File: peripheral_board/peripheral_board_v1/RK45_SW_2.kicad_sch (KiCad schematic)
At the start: 10 parts

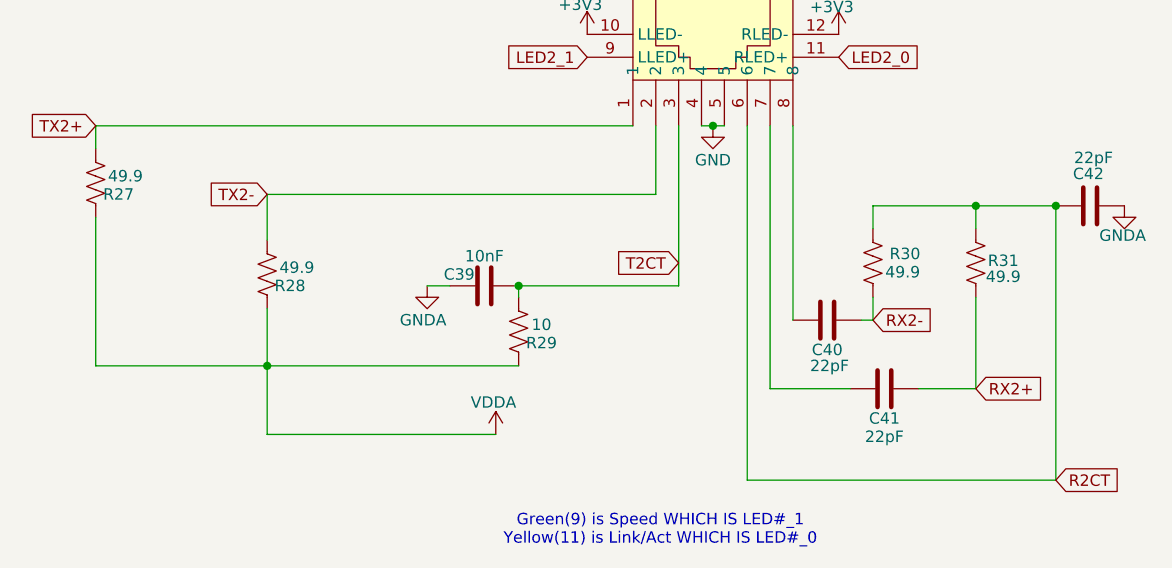
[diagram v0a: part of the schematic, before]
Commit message: Update to the board
Changed the WIZNET configuration to match that of the Pico2 eval board.
Changed the some names and some layout of the page. Not too much besides copying, reading as to why it is they way they made it and then applying.
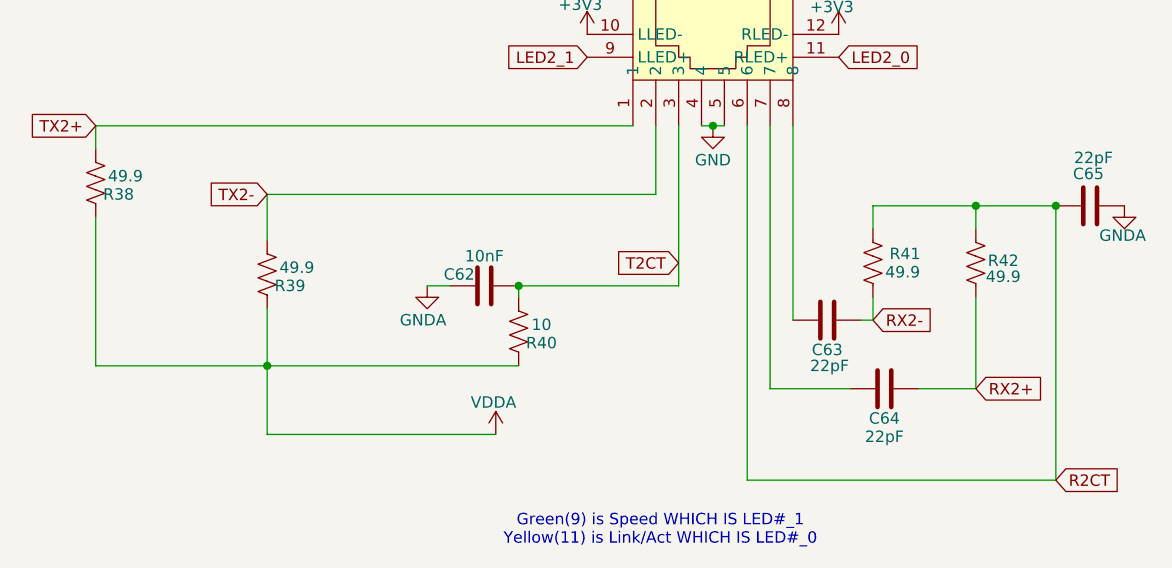
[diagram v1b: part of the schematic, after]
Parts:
- renumbered C39 to C62, C40 to C63, C41 to C64, C42 to C65, R27 to R38, R28 to R39, R29 to R40, R30 to R41, R31 to R42
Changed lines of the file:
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@@
 		(on_board yes)
 		(dnp no)
-		(property "Reference" "#PWR088"
+		(property "Reference" "#PWR0119"
 			(at 250.19 110.49 0)
 			(effects
@@
 			(project "peripheral_board"
 				(path "/14f8712f-1710-40cb-b01e-cc9b3c4405bd/bdffb641-9271-40a7-b849-e20d9ae38619/e33b6a68-dc96-48cc-8464-e4dc3509a86a"
-					(reference "#PWR088")
+					(reference "#PWR0119")
 					(unit 1)
 				)
@@
 		(on_board yes)
 		(dnp no)
-		(property "Reference" "#PWR086"
+		(property "Reference" "#PWR0117"
 			(at 236.22 123.19 0)
 			(effects
@@
 			(project "peripheral_board"
 				(path "/14f8712f-1710-40cb-b01e-cc9b3c4405bd/bdffb641-9271-40a7-b849-e20d9ae38619/e33b6a68-dc96-48cc-8464-e4dc3509a86a"
-					(reference "#PWR086")
+					(reference "#PWR0117")
 					(unit 1)
 				)
@@
 		(on_board yes)
 		(dnp no)
-		(property "Reference" "R28"
+		(property "Reference" "R39"
 			(at 189.23 134.62 0)
 			(effects
@@
 			(project "peripheral_board"
 				(path "/14f8712f-1710-40cb-b01e-cc9b3c4405bd/bdffb641-9271-40a7-b849-e20d9ae38619/e33b6a68-dc96-48cc-8464-e4dc3509a86a"
-					(reference "R28")
+					(reference "R39")
 					(unit 1)
 				)
@@
 		(on_board yes)
 		(dnp no)
-		(property "Reference" "R31"
+		(property "Reference" "R42"
 			(at 268.478 131.826 0)
 			(effects
@@
 			(project "peripheral_board"
 				(path "/14f8712f-1710-40cb-b01e-cc9b3c4405bd/bdffb641-9271-40a7-b849-e20d9ae38619/e33b6a68-dc96-48cc-8464-e4dc3509a86a"
-					(reference "R31")
+					(reference "R42")
 					(unit 1)
 				)
@@
 		(on_board yes)
 		(dnp no)
-		(property "Reference" "#PWR085"
+		(property "Reference" "#PWR0116"
 			(at 222.25 110.49 0)
 			(effects
@@
 			(project "peripheral_board"
 				(path "/14f8712f-1710-40cb-b01e-cc9b3c4405bd/bdffb641-9271-40a7-b849-e20d9ae38619/e33b6a68-dc96-48cc-8464-e4dc3509a86a"
-					(reference "#PWR085")
+					(reference "#PWR0116")
 					(unit 1)
 				)
@@
 		(on_board yes)
 		(dnp no)
-		(property "Reference" "C40"
+		(property "Reference" "C63"
 			(at 248.92 141.732 90)
 			(effects
@@
 			(project "peripheral_board"
 				(path "/14f8712f-1710-40cb-b01e-cc9b3c4405bd/bdffb641-9271-40a7-b849-e20d9ae38619/e33b6a68-dc96-48cc-8464-e4dc3509a86a"
-					(reference "C40")
+					(reference "C63")
 					(unit 1)
 				)
@@
 		(on_board yes)
 		(dnp no)
-		(property "Reference" "#PWR082"
+		(property "Reference" "#PWR0113"
 			(at 204.47 140.97 0)
 			(effects
@@
 			(project "peripheral_board"
 				(path "/14f8712f-1710-40cb-b01e-cc9b3c4405bd/bdffb641-9271-40a7-b849-e20d9ae38619/e33b6a68-dc96-48cc-8464-e4dc3509a86a"
-					(reference "#PWR082")
+					(reference "#PWR0113")
 					(unit 1)
 				)
@@
 		(on_board yes)
 		(dnp no)
-		(property "Reference" "R30"
+		(property "Reference" "R41"
 			(at 257.556 131.064 0)
 			(effects
@@
 			(project "peripheral_board"
 				(path "/14f8712f-1710-40cb-b01e-cc9b3c4405bd/bdffb641-9271-40a7-b849-e20d9ae38619/e33b6a68-dc96-48cc-8464-e4dc3509a86a"
-					(reference "R30")
+					(reference "R41")
 					(unit 1)
 				)
@@
 		(on_board yes)
 		(dnp no)
-		(property "Reference" "C39"
+		(property "Reference" "C62"
 			(at 208.026 133.35 90)
 			(effects
@@
 			(project "peripheral_board"
 				(path "/14f8712f-1710-40cb-b01e-cc9b3c4405bd/bdffb641-9271-40a7-b849-e20d9ae38619/e33b6a68-dc96-48cc-8464-e4dc3509a86a"
-					(reference "C39")
+					(reference "C62")
 					(unit 1)
 				)
@@
 		(on_board yes)
 		(dnp no)
-		(property "Reference" "#PWR084"
+		(property "Reference" "#PWR0115"
 			(at 222.25 102.87 0)
 			(effects
@@
 			(project "peripheral_board"
 				(path "/14f8712f-1710-40cb-b01e-cc9b3c4405bd/bdffb641-9271-40a7-b849-e20d9ae38619/e33b6a68-dc96-48cc-8464-e4dc3509a86a"
-					(reference "#PWR084")
+					(reference "#PWR0115")
 					(unit 1)
 				)
@@
 		(on_board yes)
 		(dnp no)
-		(property "Reference" "R29"
+		(property "Reference" "R40"
 			(at 217.17 140.97 0)
 			(effects
@@
 			(project "peripheral_board"
 				(path "/14f8712f-1710-40cb-b01e-cc9b3c4405bd/bdffb641-9271-40a7-b849-e20d9ae38619/e33b6a68-dc96-48cc-8464-e4dc3509a86a"
-					(reference "R29")
+					(reference "R40")
 					(unit 1)
 				)
@@
 		(on_board yes)
 		(dnp no)
-		(property "Reference" "#PWR087"
+		(property "Reference" "#PWR0118"
 			(at 250.19 102.87 0)
 			(effects
@@
 			(project "peripheral_board"
 				(path "/14f8712f-1710-40cb-b01e-cc9b3c4405bd/bdffb641-9271-40a7-b849-e20d9ae38619/e33b6a68-dc96-48cc-8464-e4dc3509a86a"
-					(reference "#PWR087")
+					(reference "#PWR0118")
 					(unit 1)
 				)
@@
 		(on_board yes)
 		(dnp no)
-		(property "Reference" "#PWR089"
+		(property "Reference" "#PWR0120"
 			(at 281.94 132.08 0)
 			(effects
@@
 			(project "peripheral_board"
 				(path "/14f8712f-1710-40cb-b01e-cc9b3c4405bd/bdffb641-9271-40a7-b849-e20d9ae38619/e33b6a68-dc96-48cc-8464-e4dc3509a86a"
-					(reference "#PWR089")
+					(reference "#PWR0120")
 					(unit 1)
 				)
@@
 		(on_board yes)
 		(dnp no)
-		(property "Reference" "C41"
+		(property "Reference" "C64"
 			(at 255.27 149.352 90)
 			(effects
@@
 			(project "peripheral_board"
 				(path "/14f8712f-1710-40cb-b01e-cc9b3c4405bd/bdffb641-9271-40a7-b849-e20d9ae38619/e33b6a68-dc96-48cc-8464-e4dc3509a86a"
-					(reference "C41")
+					(reference "C64")
 					(unit 1)
 				)
@@
 		(on_board yes)
 		(dnp no)
-		(property "Reference" "C42"
+		(property "Reference" "C65"
 			(at 279.654 122.174 90)
 			(effects
@@
 			(project "peripheral_board"
 				(path "/14f8712f-1710-40cb-b01e-cc9b3c4405bd/bdffb641-9271-40a7-b849-e20d9ae38619/e33b6a68-dc96-48cc-8464-e4dc3509a86a"
-					(reference "C42")
+					(reference "C65")
 					(unit 1)
 				)
@@
 		(on_board yes)
 		(dnp no)
-		(property "Reference" "R27"
+		(property "Reference" "R38"
 			(at 170.18 124.46 0)
 			(effects
@@
 			(project "peripheral_board"
 				(path "/14f8712f-1710-40cb-b01e-cc9b3c4405bd/bdffb641-9271-40a7-b849-e20d9ae38619/e33b6a68-dc96-48cc-8464-e4dc3509a86a"
-					(reference "R27")
+					(reference "R38")
 					(unit 1)
 				)
@@
 		(on_board yes)
 		(dnp no)
-		(property "Reference" "#PWR083"
+		(property "Reference" "#PWR0114"
 			(at 212.09 154.94 0)
 			(effects
@@
 			(project "peripheral_board"
 				(path "/14f8712f-1710-40cb-b01e-cc9b3c4405bd/bdffb641-9271-40a7-b849-e20d9ae38619/e33b6a68-dc96-48cc-8464-e4dc3509a86a"
-					(reference "#PWR083")
-					(unit 1)
-				)
+					(reference "#PWR0114")
+					(unit 1)
+				)

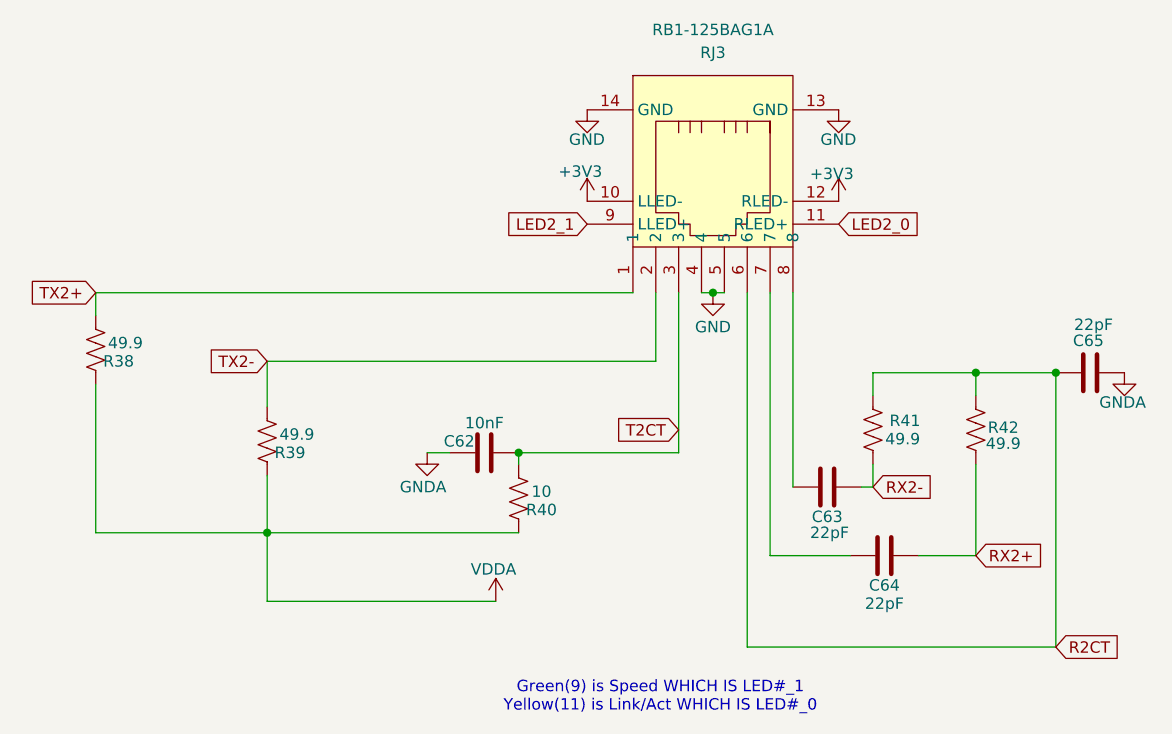
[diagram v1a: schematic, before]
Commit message: Update to the PCB
#Changes made so far

## Wiznet
* Changed the Wiznet layout to match that of their development board
* Restructured the RJ45 connections
    * *Looked over the RJ45 still a unsure*
    * Added in 2 differnt versions of Ethernt Connections. The one that shows the magnetics might be used for the Ethernet switch.
* Removed the Single Bus Buffer gate with 3-state output to match the dev board

## Raspberry Pi
* Moved to USB type C from micro USB for debugging.
* Changed the GPIO pins to match the Wiznet dev board.
* Brought in breakout pins for the rest of the GPIO.
* Cleaned up the Schematic to make it more clean.

## Ethernet Switch
* Changed the crystal to be the same as the Wiznet and to have the correct load caps
* Looking at the design check list to help get moving forward, need to relook at power distribution.
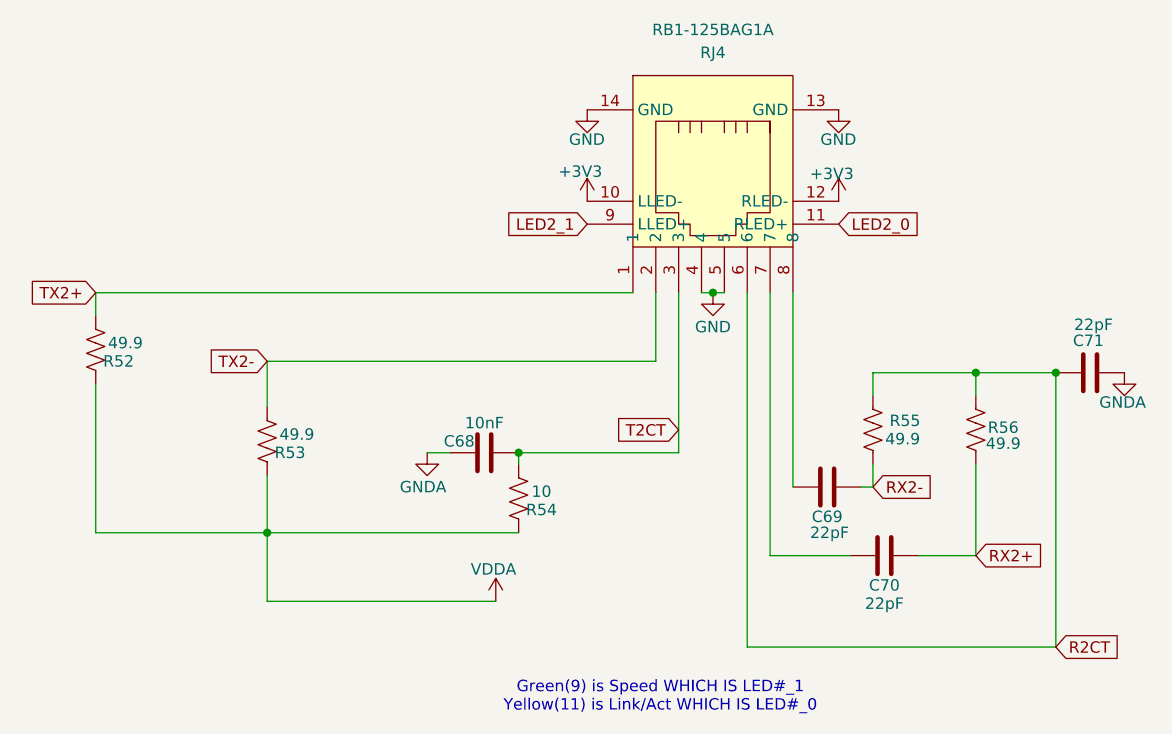
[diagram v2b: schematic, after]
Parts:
- renumbered C62 to C68, C63 to C69, C64 to C70, C65 to C71, R38 to R52, R39 to R53, R40 to R54, R41 to R55, R42 to R56, RJ3 to RJ4
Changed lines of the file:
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@@
 		(on_board yes)
 		(dnp no)
-		(property "Reference" "#PWR0119"
+		(property "Reference" "#PWR0133"
 			(at 250.19 110.49 0)
 			(effects
@@
 			(project "peripheral_board"
 				(path "/14f8712f-1710-40cb-b01e-cc9b3c4405bd/bdffb641-9271-40a7-b849-e20d9ae38619/e33b6a68-dc96-48cc-8464-e4dc3509a86a"
-					(reference "#PWR0119")
+					(reference "#PWR0133")
 					(unit 1)
 				)
@@
 		(on_board yes)
 		(dnp no)
-		(property "Reference" "#PWR0117"
+		(property "Reference" "#PWR0131"
 			(at 236.22 123.19 0)
 			(effects
@@
 			(project "peripheral_board"
 				(path "/14f8712f-1710-40cb-b01e-cc9b3c4405bd/bdffb641-9271-40a7-b849-e20d9ae38619/e33b6a68-dc96-48cc-8464-e4dc3509a86a"
-					(reference "#PWR0117")
+					(reference "#PWR0131")
 					(unit 1)
 				)
@@
 		(on_board yes)
 		(dnp no)
-		(property "Reference" "R39"
+		(property "Reference" "R53"
 			(at 189.23 134.62 0)
 			(effects
@@
 			(project "peripheral_board"
 				(path "/14f8712f-1710-40cb-b01e-cc9b3c4405bd/bdffb641-9271-40a7-b849-e20d9ae38619/e33b6a68-dc96-48cc-8464-e4dc3509a86a"
-					(reference "R39")
+					(reference "R53")
 					(unit 1)
 				)
@@
 		(on_board yes)
 		(dnp no)
-		(property "Reference" "R42"
+		(property "Reference" "R56"
 			(at 268.478 131.826 0)
 			(effects
@@
 			(project "peripheral_board"
 				(path "/14f8712f-1710-40cb-b01e-cc9b3c4405bd/bdffb641-9271-40a7-b849-e20d9ae38619/e33b6a68-dc96-48cc-8464-e4dc3509a86a"
-					(reference "R42")
+					(reference "R56")
 					(unit 1)
 				)
@@
 		(dnp no)
 		(fields_autoplaced yes)
-		(property "Reference" "RJ3"
+		(property "Reference" "RJ4"
 			(at 236.22 90.17 0)
 			(effects
@@
 			(project "peripheral_board"
 				(path "/14f8712f-1710-40cb-b01e-cc9b3c4405bd/bdffb641-9271-40a7-b849-e20d9ae38619/e33b6a68-dc96-48cc-8464-e4dc3509a86a"
-					(reference "RJ3")
+					(reference "RJ4")
 					(unit 1)
 				)
@@
 		(on_board yes)
 		(dnp no)
-		(property "Reference" "#PWR0116"
+		(property "Reference" "#PWR0130"
 			(at 222.25 110.49 0)
 			(effects
@@
 			(project "peripheral_board"
 				(path "/14f8712f-1710-40cb-b01e-cc9b3c4405bd/bdffb641-9271-40a7-b849-e20d9ae38619/e33b6a68-dc96-48cc-8464-e4dc3509a86a"
-					(reference "#PWR0116")
+					(reference "#PWR0130")
 					(unit 1)
 				)
@@
 		(on_board yes)
 		(dnp no)
-		(property "Reference" "C63"
+		(property "Reference" "C69"
 			(at 248.92 141.732 90)
 			(effects
@@
 			(project "peripheral_board"
 				(path "/14f8712f-1710-40cb-b01e-cc9b3c4405bd/bdffb641-9271-40a7-b849-e20d9ae38619/e33b6a68-dc96-48cc-8464-e4dc3509a86a"
-					(reference "C63")
+					(reference "C69")
 					(unit 1)
 				)
@@
 		(on_board yes)
 		(dnp no)
-		(property "Reference" "#PWR0113"
+		(property "Reference" "#PWR0127"
 			(at 204.47 140.97 0)
 			(effects
@@
 			(project "peripheral_board"
 				(path "/14f8712f-1710-40cb-b01e-cc9b3c4405bd/bdffb641-9271-40a7-b849-e20d9ae38619/e33b6a68-dc96-48cc-8464-e4dc3509a86a"
-					(reference "#PWR0113")
+					(reference "#PWR0127")
 					(unit 1)
 				)
@@
 		(on_board yes)
 		(dnp no)
-		(property "Reference" "R41"
+		(property "Reference" "R55"
 			(at 257.556 131.064 0)
 			(effects
@@
 			(project "peripheral_board"
 				(path "/14f8712f-1710-40cb-b01e-cc9b3c4405bd/bdffb641-9271-40a7-b849-e20d9ae38619/e33b6a68-dc96-48cc-8464-e4dc3509a86a"
-					(reference "R41")
+					(reference "R55")
 					(unit 1)
 				)
@@
 		(on_board yes)
 		(dnp no)
-		(property "Reference" "C62"
+		(property "Reference" "C68"
 			(at 208.026 133.35 90)
 			(effects
@@
 			(project "peripheral_board"
 				(path "/14f8712f-1710-40cb-b01e-cc9b3c4405bd/bdffb641-9271-40a7-b849-e20d9ae38619/e33b6a68-dc96-48cc-8464-e4dc3509a86a"
-					(reference "C62")
+					(reference "C68")
 					(unit 1)
 				)
@@
 		(on_board yes)
 		(dnp no)
-		(property "Reference" "#PWR0115"
+		(property "Reference" "#PWR0129"
 			(at 222.25 102.87 0)
 			(effects
@@
 			(project "peripheral_board"
 				(path "/14f8712f-1710-40cb-b01e-cc9b3c4405bd/bdffb641-9271-40a7-b849-e20d9ae38619/e33b6a68-dc96-48cc-8464-e4dc3509a86a"
-					(reference "#PWR0115")
+					(reference "#PWR0129")
 					(unit 1)
 				)
@@
 		(on_board yes)
 		(dnp no)
-		(property "Reference" "R40"
+		(property "Reference" "R54"
 			(at 217.17 140.97 0)
 			(effects
@@
 			(project "peripheral_board"
 				(path "/14f8712f-1710-40cb-b01e-cc9b3c4405bd/bdffb641-9271-40a7-b849-e20d9ae38619/e33b6a68-dc96-48cc-8464-e4dc3509a86a"
-					(reference "R40")
+					(reference "R54")
 					(unit 1)
 				)
@@
 		(on_board yes)
 		(dnp no)
-		(property "Reference" "#PWR0118"
+		(property "Reference" "#PWR0132"
 			(at 250.19 102.87 0)
 			(effects
@@
 			(project "peripheral_board"
 				(path "/14f8712f-1710-40cb-b01e-cc9b3c4405bd/bdffb641-9271-40a7-b849-e20d9ae38619/e33b6a68-dc96-48cc-8464-e4dc3509a86a"
-					(reference "#PWR0118")
+					(reference "#PWR0132")
 					(unit 1)
 				)
@@
 		(on_board yes)
 		(dnp no)
-		(property "Reference" "#PWR0120"
+		(property "Reference" "#PWR0134"
 			(at 281.94 132.08 0)
 			(effects
@@
 			(project "peripheral_board"
 				(path "/14f8712f-1710-40cb-b01e-cc9b3c4405bd/bdffb641-9271-40a7-b849-e20d9ae38619/e33b6a68-dc96-48cc-8464-e4dc3509a86a"
-					(reference "#PWR0120")
+					(reference "#PWR0134")
 					(unit 1)
 				)
@@
 		(on_board yes)
 		(dnp no)
-		(property "Reference" "C64"
+		(property "Reference" "C70"
 			(at 255.27 149.352 90)
 			(effects
@@
 			(project "peripheral_board"
 				(path "/14f8712f-1710-40cb-b01e-cc9b3c4405bd/bdffb641-9271-40a7-b849-e20d9ae38619/e33b6a68-dc96-48cc-8464-e4dc3509a86a"
-					(reference "C64")
+					(reference "C70")
 					(unit 1)
 				)
@@
 		(on_board yes)
 		(dnp no)
-		(property "Reference" "C65"
+		(property "Reference" "C71"
 			(at 279.654 122.174 90)
 			(effects
@@
 			(project "peripheral_board"
 				(path "/14f8712f-1710-40cb-b01e-cc9b3c4405bd/bdffb641-9271-40a7-b849-e20d9ae38619/e33b6a68-dc96-48cc-8464-e4dc3509a86a"
-					(reference "C65")
+					(reference "C71")
 					(unit 1)
 				)
@@
 		(on_board yes)
 		(dnp no)
-		(property "Reference" "R38"
+		(property "Reference" "R52"
 			(at 170.18 124.46 0)
 			(effects
@@
 			(project "peripheral_board"
 				(path "/14f8712f-1710-40cb-b01e-cc9b3c4405bd/bdffb641-9271-40a7-b849-e20d9ae38619/e33b6a68-dc96-48cc-8464-e4dc3509a86a"
-					(reference "R38")
+					(reference "R52")
 					(unit 1)
 				)
@@
 		(on_board yes)
 		(dnp no)
-		(property "Reference" "#PWR0114"
+		(property "Reference" "#PWR0128"
 			(at 212.09 154.94 0)
 			(effects
@@
 			(project "peripheral_board"
 				(path "/14f8712f-1710-40cb-b01e-cc9b3c4405bd/bdffb641-9271-40a7-b849-e20d9ae38619/e33b6a68-dc96-48cc-8464-e4dc3509a86a"
-					(reference "#PWR0114")
-					(unit 1)
-				)
+					(reference "#PWR0128")
+					(unit 1)
+				)
